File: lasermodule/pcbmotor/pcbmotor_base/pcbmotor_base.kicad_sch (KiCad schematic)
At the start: 16 parts, among them J15 Conn_01x01, J16 Conn_01x01, J17 Conn_01x01, J4 Conn_01x03, J5 Conn_01x13, U1 MP6543HGL-A-P, U6 DRV5033FAxDBZ, U7 DRV5033FAxDBZ, U8 DRV5033FAxDBZ

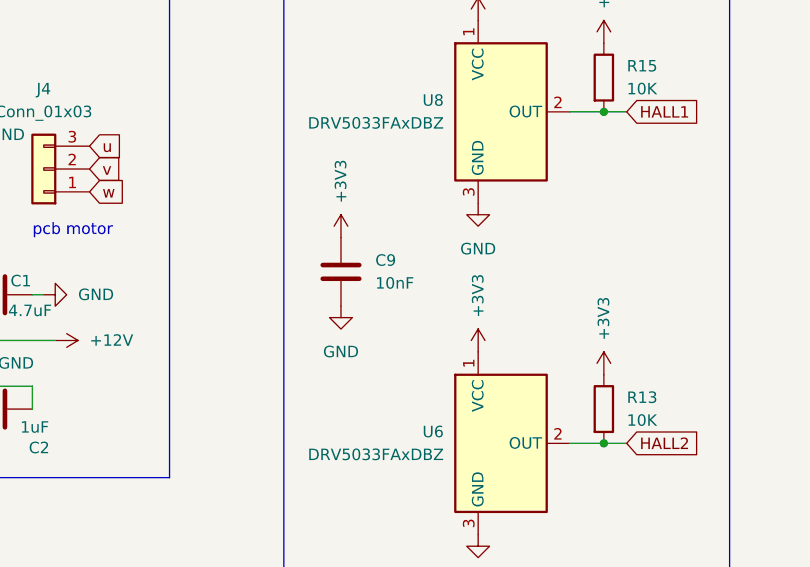
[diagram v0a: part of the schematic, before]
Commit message: fixed boms, small modifications to the boards.
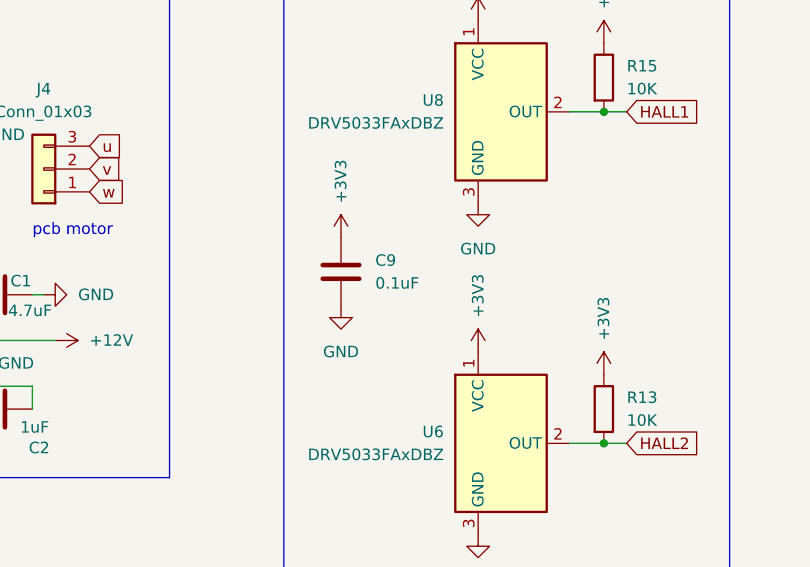
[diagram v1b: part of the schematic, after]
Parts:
- C1: farnell# (none) -> 2611942; manf# (none) -> GRM21BR61H475KE51L; mouser# (none) -> 81-GRM21BR61H475KE1L
- C2: farnell# (none) -> 2094043; manf# (none) -> 08055C105KAT2A; mouser# (none) -> 581-08055C105KAT2A
- C9: value 10nF -> 0.1uF; farnell# (none) -> 1414663; manf# (none) -> C0805C104J5RACTU; mouser# (none) -> 80-C0805C104J5R
- R13, R14: manf# (none) -> CRCW080510K0JNEAC; mouser# (none) -> 71-CRCW080510K0JNEAC
- R15: farnell# (none) -> 2826162; manf# (none) -> CRCW080510K0JNEAC; mouser# (none) -> 71-CRCW080510K0JNEAC
- U1: manf# (none) -> MP6543HGL-A-P; manuf# MP6543HGL-A-P -> (none)
- U6, U7: manf# (none) -> DRV5033FAQDBZR; mouser# (none) -> 595-RV5033FAEDBZRQ1
- U8: farnell# (none) -> 3006067; manf# (none) -> DRV5033FAQDBZR; mouser# (none) -> 595-RV5033FAEDBZRQ1

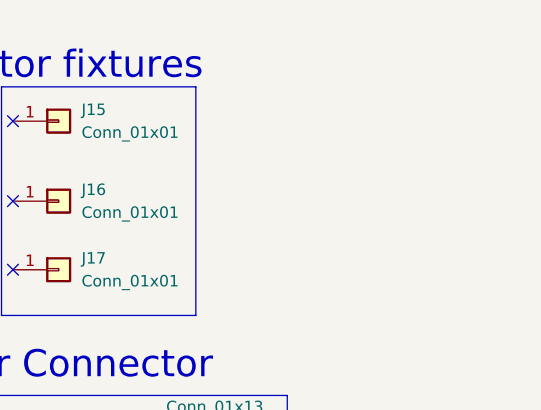
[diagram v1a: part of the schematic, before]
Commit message: improved connection between pcb motor and base plate
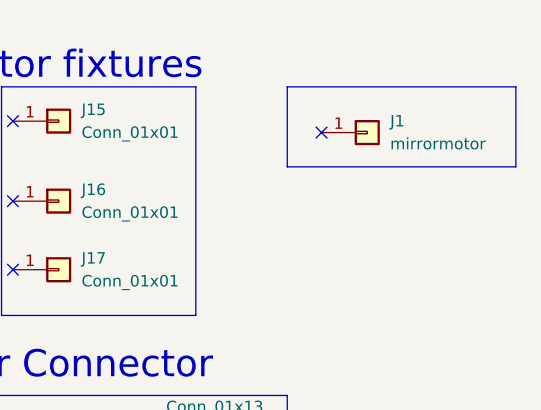
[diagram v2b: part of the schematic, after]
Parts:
- added J1: mirrormotor, sockets_scanhead:mirror_motor, symbol Connector_Generic:Conn_01x01
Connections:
- no-connect marks 10 -> 11
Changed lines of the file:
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@@
+	)
+	(no_connect
+		(at 241.3 34.29)
 	)
 	(no_connect
@@
 		)
 	)
+	(polyline
+		(pts
+			(xy 262.89 38.1) (xy 262.89 29.21)
+		)
+		(stroke
+			(width 0)
+			(type default)
+		)
+	)
 	(wire
 		(pts
@@
 	(polyline
 		(pts
+			(xy 262.89 29.21) (xy 237.49 29.21)
+		)
+		(stroke
+			(width 0)
+			(type default)
+		)
+	)
+	(polyline
+		(pts
 			(xy 237.49 63.5) (xy 195.58 63.5)
 		)
@@
 	(polyline
 		(pts
+			(xy 237.49 38.1) (xy 262.89 38.1)
+		)
+		(stroke
+			(width 0)
+			(type default)
+		)
+	)
+	(polyline
+		(pts
 			(xy 43.18 27.94) (xy 43.18 87.63)
 		)
@@
 		(pts
 			(xy 210.82 83.82) (xy 224.79 83.82)
+		)
+		(stroke
+			(width 0)
+			(type default)
+		)
+	)
+	(polyline
+		(pts
+			(xy 237.49 29.21) (xy 237.49 38.1)
 		)
 		(stroke
@@
 					(unit 1)
 				)
+			)
+		)
+	)
+	(symbol
+		(lib_id "Connector_Generic:Conn_01x01")
+		(at 246.38 34.29 0)
+		(unit 1)
+		(exclude_from_sim no)
+		(in_bom yes)
+		(on_board yes)
+		(dnp no)
+		(fields_autoplaced yes)
+		(property "Reference" "J1"
+			(at 248.92 33.0199 0)
+			(effects
+				(font
+					(size 1.27 1.27)
+				)
+				(justify left)
+			)
+		)
+		(property "Value" "mirrormotor"
+			(at 248.92 35.5599 0)
+			(effects
+				(font
+					(size 1.27 1.27)
+				)
+				(justify left)
+			)
+		)
+		(property "Footprint" "sockets_scanhead:mirror_motor"
+			(at 246.38 34.29 0)
+			(effects
+				(font
+					(size 1.27 1.27)
+				)
+				(hide yes)
+			)
+		)
+		(property "Datasheet" "~"
+			(at 246.38 34.29 0)
+			(effects
+				(font
+					(size 1.27 1.27)
+				)
+				(hide yes)
+			)
+		)
+		(property "Description" ""
+			(at 246.38 34.29 0)
+			(effects
+				(font
+					(size 1.27 1.27)
+				)
+				(hide yes)
+			)
+		)
+		(pin "1"
+		)
+		(instances
+			(project "pcbmotor_base"
+				(path "/6ad206d4-5372-46a2-80b5-cf4f27c341ba"
+					(reference "J1")
+					(unit 1)
+				)
